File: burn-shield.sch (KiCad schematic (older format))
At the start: 3 parts, among them J1 28 ZIF Socket

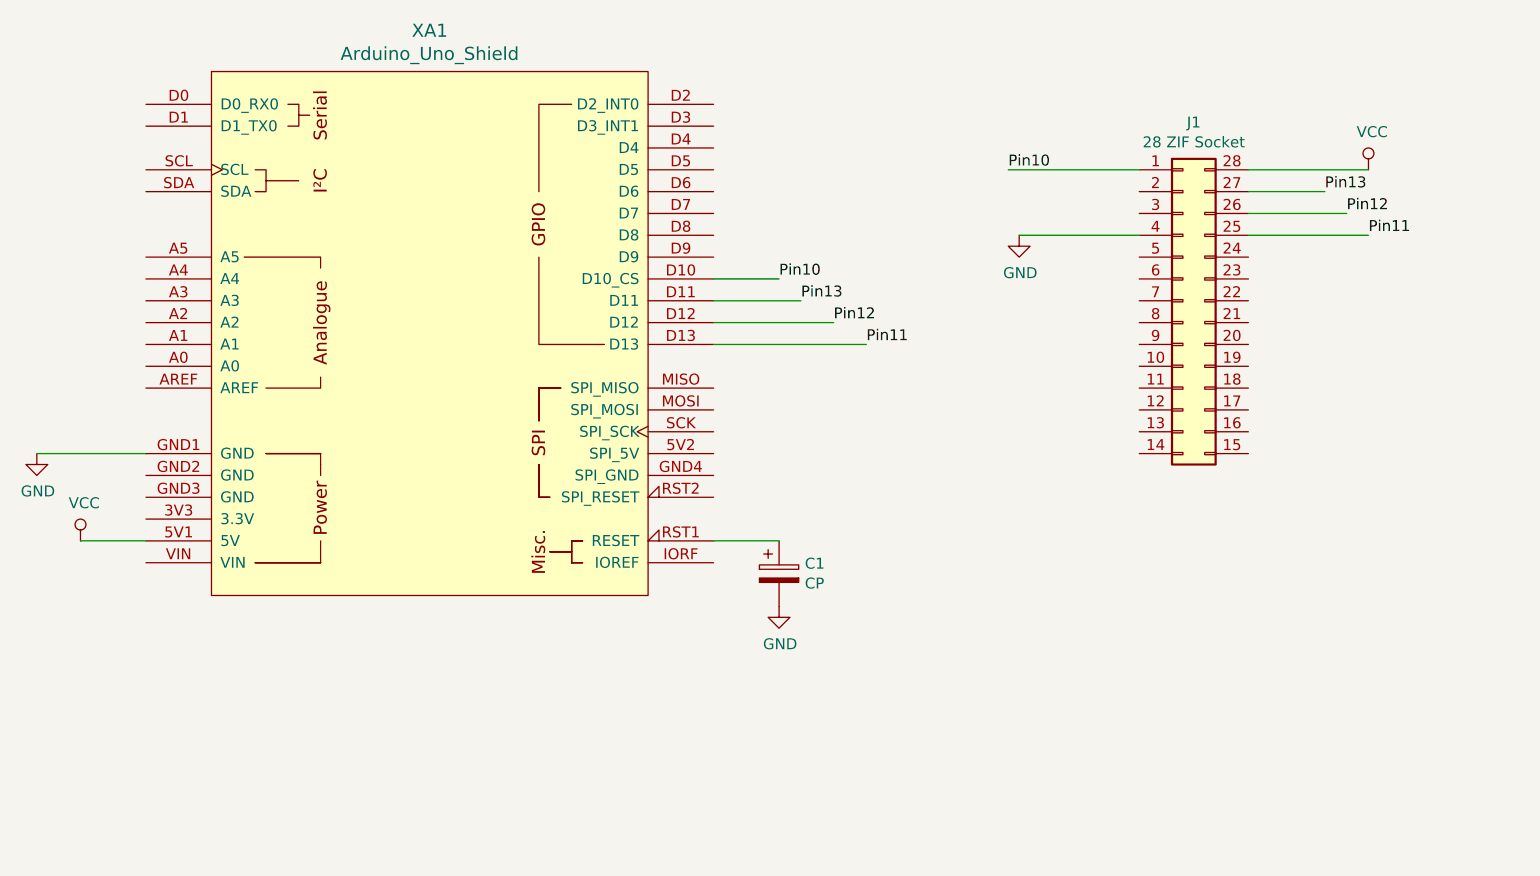
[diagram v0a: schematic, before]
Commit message: Added the ATMEGA support too
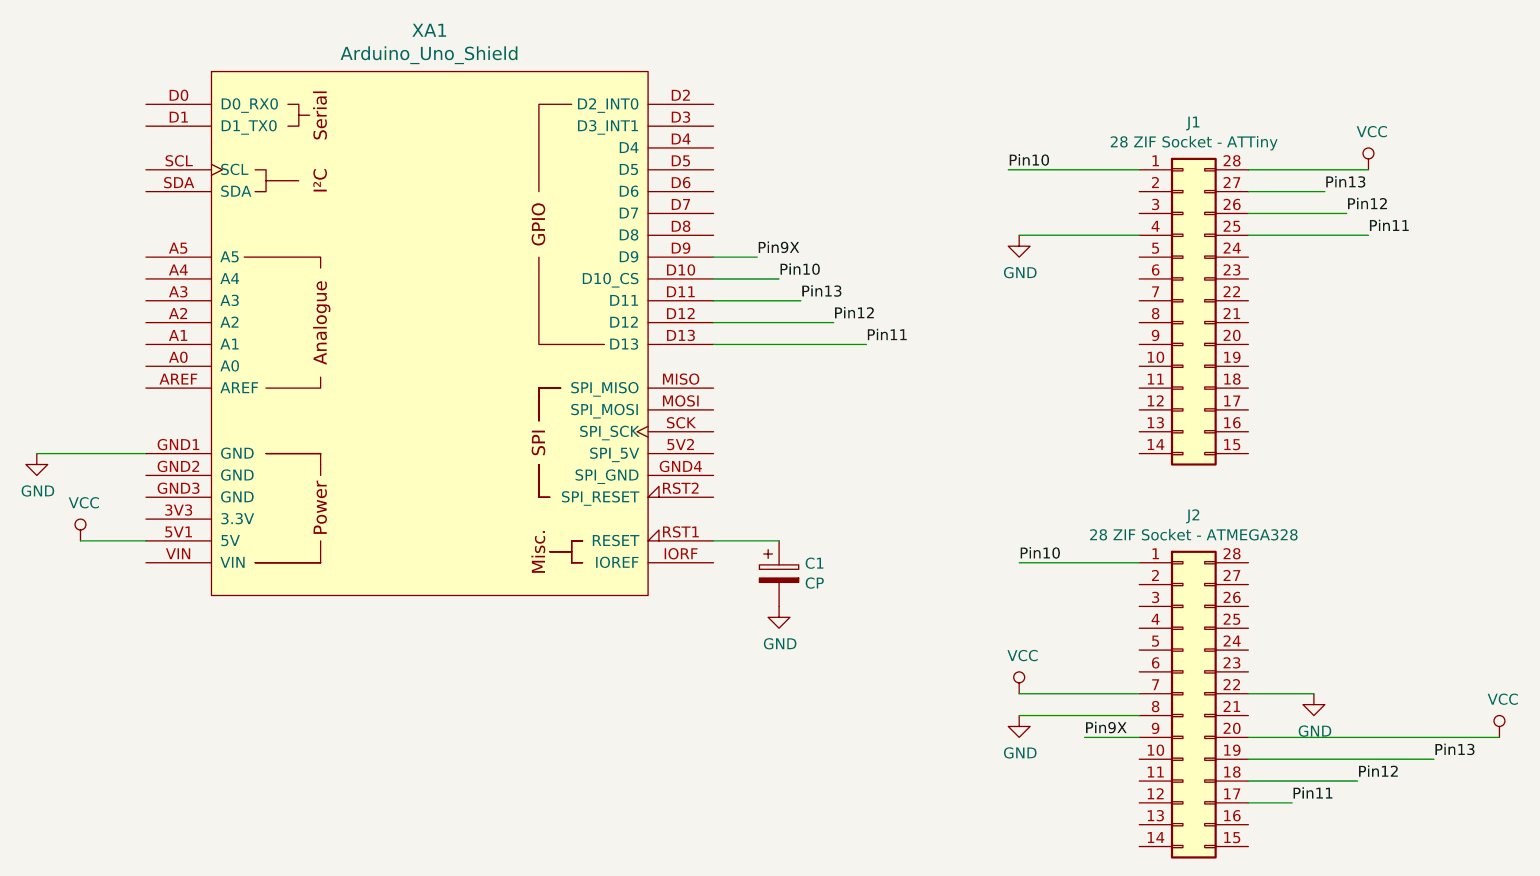
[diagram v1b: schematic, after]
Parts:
- added J2: 28 ZIF Socket - ATMEGA328, ZIF:DIP-28_296_ELL, symbol Connector_Generic:Conn_02x14_Counter_Clockwise
- J1: value 28 ZIF Socket -> 28 ZIF Socket - ATTiny; footprint ZIF:ZIF-DIP-28_98 -> ZIF:DIP-28_296_ELL
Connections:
- net GND: now also J2.22 (Pin_22), J2.8 (Pin_8)
- net Pin10: now also J2.1 (Pin_1)
- net Pin11: now also J2.17 (Pin_17)
- net Pin12: now also J2.18 (Pin_18)
- net Pin13: now also J2.19 (Pin_19)
- net VCC: now also J2.20 (Pin_20), J2.7 (Pin_7)
- net Pin9X: now reaches XA1.D9
- net Pin9X: now also J2.9 (Pin_9)
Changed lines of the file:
@@
 EESchema Schematic File Version 4
+LIBS:burn-shield-cache
 EELAYER 29 0
 EELAYER END
@@
 P 7600 3400
 F 0 "J1" H 7650 4217 50  0000 C CNN
-F 1 "28 ZIF Socket" H 7650 4126 50  0000 C CNN
-F 2 "ZIF:ZIF-DIP-28_98" H 7600 3400 50  0001 C CNN
+F 1 "28 ZIF Socket - ATTiny" H 7650 4126 50  0000 C CNN
+F 2 "ZIF:DIP-28_296_ELL" H 7600 3400 50  0001 C CNN
 F 3 "~" H 7600 3400 50  0001 C CNN
 	1    7600 3400
@@
 Text Label 6150 3600 0    50   ~ 0
 Pin11
+$Comp
+L Connector_Generic:Conn_02x14_Counter_Clockwise J2
+U 1 1 5FECDADE
+P 7600 5200
+F 0 "J2" H 7650 6017 50  0000 C CNN
+F 1 "28 ZIF Socket - ATMEGA328" H 7650 5926 50  0000 C CNN
+F 2 "ZIF:DIP-28_296_ELL" H 7600 5200 50  0001 C CNN
+F 3 "~" H 7600 5200 50  0001 C CNN
+	1    7600 5200
+	1    0    0    -1
+$EndComp
+Wire Wire Line
+	7400 4600 6850 4600
+Text Label 6850 4600 0    50   ~ 0
+Pin10
+Wire Wire Line
+	7400 5200 6850 5200
+$Comp
+L power:VCC #PWR06
+U 1 1 5FED1E26
+P 6850 5200
+F 0 "#PWR06" H 6850 5050 50  0001 C CNN
+F 1 "VCC" H 6867 5373 50  0000 C CNN
+F 2 "" H 6850 5200 50  0001 C CNN
+F 3 "" H 6850 5200 50  0001 C CNN
+	1    6850 5200
+	1    0    0    -1
+$EndComp
+Wire Wire Line
+	7400 5300 6850 5300
+$Comp
+L power:GND #PWR07
+U 1 1 5FED2E7C
+P 6850 5300
+F 0 "#PWR07" H 6850 5050 50  0001 C CNN
+F 1 "GND" H 6855 5127 50  0000 C CNN
+F 2 "" H 6850 5300 50  0001 C CNN
+F 3 "" H 6850 5300 50  0001 C CNN
+	1    6850 5300
+	1    0    0    -1
+$EndComp
+Wire Wire Line
+	7400 5400 7150 5400
+Wire Wire Line
+	5450 3200 5650 3200
+Text Label 5650 3200 0    50   ~ 0
+Pin9X
+Text Label 7150 5400 0    50   ~ 0
+Pin9X
+Wire Wire Line
+	7900 5700 8100 5700
+Text Label 8100 5700 0    50   ~ 0
+Pin11
+Wire Wire Line
+	7900 5600 8400 5600
+Text Label 8400 5600 0    50   ~ 0
+Pin12
+Wire Wire Line
+	7900 5500 8750 5500
+Text Label 8750 5500 0    50   ~ 0
+Pin13
+Wire Wire Line
+	7900 5400 9050 5400
+$Comp
+L power:VCC #PWR09
+U 1 1 5FED5A01
+P 9050 5400
+F 0 "#PWR09" H 9050 5250 50  0001 C CNN
+F 1 "VCC" H 9067 5573 50  0000 C CNN
+F 2 "" H 9050 5400 50  0001 C CNN
+F 3 "" H 9050 5400 50  0001 C CNN
+	1    9050 5400
+	1    0    0    -1
+$EndComp
+Wire Wire Line
+	7900 5200 8200 5200
+$Comp
+L power:GND #PWR08
+U 1 1 5FED70BA
+P 8200 5200
+F 0 "#PWR08" H 8200 4950 50  0001 C CNN
+F 1 "GND" H 8205 5027 50  0000 C CNN
+F 2 "" H 8200 5200 50  0001 C CNN
+F 3 "" H 8200 5200 50  0001 C CNN
+	1    8200 5200
+	1    0    0    -1
+$EndComp
 $EndSCHEMATC
